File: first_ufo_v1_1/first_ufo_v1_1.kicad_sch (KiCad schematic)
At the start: 66 parts, among them J2 Barrel_Jack_Switch, Q1 2N3904, SW1 SMTS-102, SW2 SMTS-102, SW3 SMTS-102, U1 40106, U3 LM358

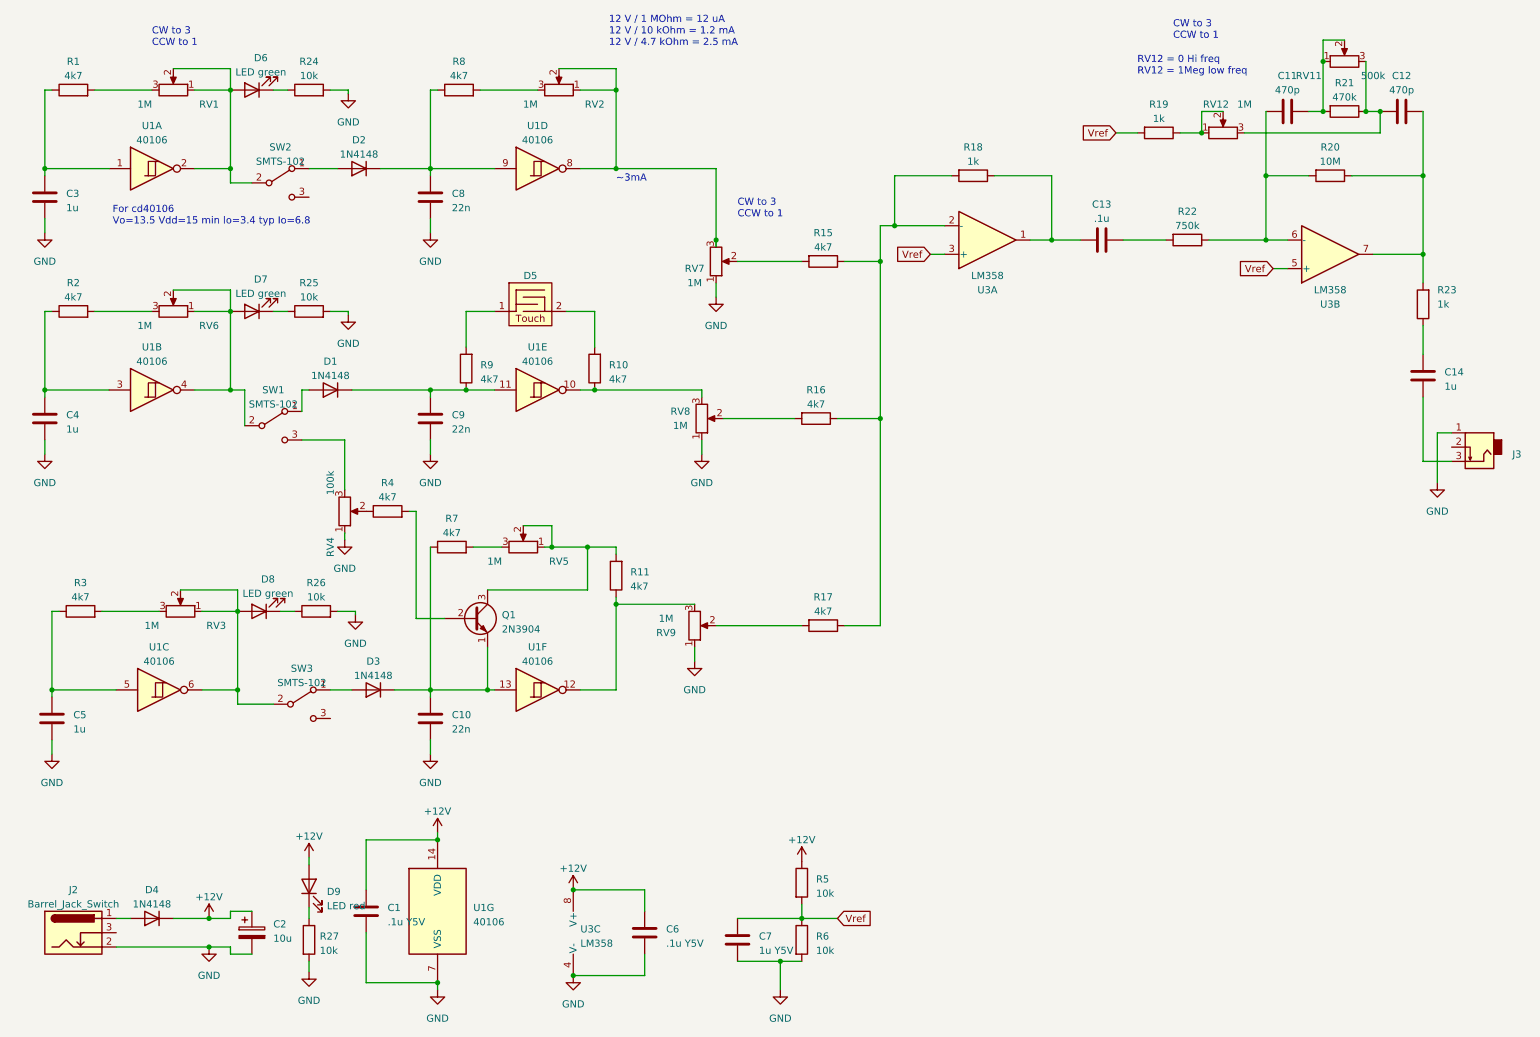
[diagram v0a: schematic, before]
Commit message: edit R15 16 17 to 27k for do not affect on freq in max volume edit RV7 8 9 for better control of volume. coz it use volatge divider now change filter for better control and range fix adder circuit. make on voltage divivder
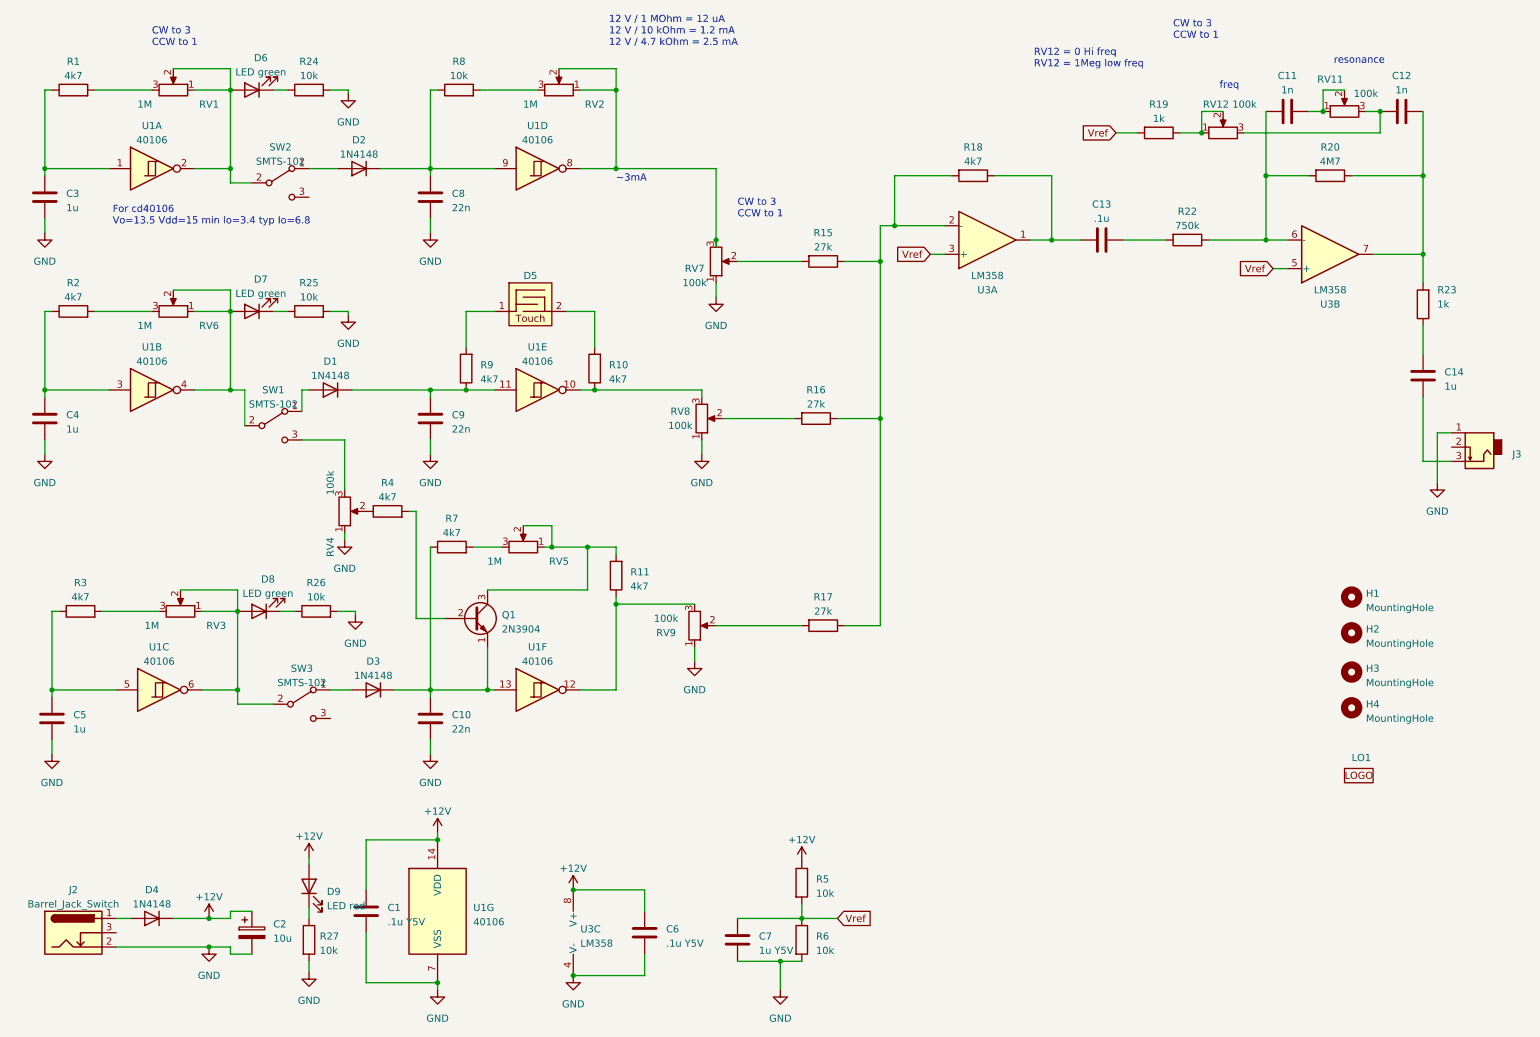
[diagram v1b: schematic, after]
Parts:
- removed R21: 470k, Resistor_THT:R_Axial_DIN0207_L6.3mm_D2.5mm_P10.16mm_Horizontal, symbol Device:R
- added H1, H2, H3, H4: MountingHole, MountingHole:MountingHole_3.2mm_M3, symbol Mechanical:MountingHole
- added LO1: ~, Symbol:Polarity_Center_Positive_6mm_SilkScreen, symbol Graphic:logo_x
- C11, C12: value 470p -> 1n
- R15, R16, R17: value 4k7 -> 27k
- R18: value 1k -> 4k7
- R20: value 10M -> 4M7
- R8: value 4k7 -> 10k
- RV11: value 500k -> 100k
- RV12, RV7, RV8, RV9: value 1M -> 100k
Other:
- note added: "freq"
- note added: "resonance"
- moved on the sheet: RV11

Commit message: no message
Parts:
- added RV10: 1M, Potentiometer_THT:Potentiometer_Bourns_PTV09A-1_Single_Vertical, symbol Device:R_Potentiometer
- LO1: footprint Symbol:Polarity_Center_Positive_6mm_SilkScreen -> Import:Polarity_Center_Positive_3mm_SilkScreen
- R1, R2, R3: value 4k7 -> 27k
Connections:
- net GND: now also RV10.1
- net at R22.2: now also RV10.2; no longer C13.2
- new net: C13.2, RV10.3
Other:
- moved on the sheet: R22
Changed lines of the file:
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@@
     (stroke (width 0) (type default))
   )
-  (wire (pts (xy 213.36 54.61) (xy 220.98 54.61))
-    (stroke (width 0) (type default))
-  )
   (wire (pts (xy 55.88 137.16) (xy 62.23 137.16))
     (stroke (width 0) (type default))
@@
     (stroke (width 0) (type default))
   )
+  (wire (pts (xy 222.25 54.61) (xy 226.06 54.61))
+    (stroke (width 0) (type default))
+  )
   (wire (pts (xy 96.52 81.28) (xy 90.17 81.28))
     (stroke (width 0) (type default))
@@
     (stroke (width 0) (type default))
   )
+  (wire (pts (xy 222.25 60.325) (xy 222.25 54.61))
+    (stroke (width 0) (type default))
+  )
   (wire (pts (xy 22.86 143.51) (xy 22.86 146.05))
     (stroke (width 0) (type default))
@@
     (stroke (width 0) (type default))
   )
+  (wire (pts (xy 216.535 56.515) (xy 216.535 54.61))
+    (stroke (width 0) (type default))
+  )
   (wire (pts (xy 100.33 127) (xy 100.33 134.62))
     (stroke (width 0) (type default))
@@
     (stroke (width 0) (type default))
   )
+  (wire (pts (xy 216.535 54.61) (xy 213.36 54.61))
+    (stroke (width 0) (type default))
+  )
   (wire (pts (xy 119.38 81.28) (xy 138.43 81.28))
     (stroke (width 0) (type default))
@@
     (stroke (width 0) (type default))
   )
+  (wire (pts (xy 216.535 64.135) (xy 216.535 66.675))
+    (stroke (width 0) (type default))
+  )
   (wire (pts (xy 179.07 57.15) (xy 181.61 57.15))
     (stroke (width 0) (type default))
@@
     (stroke (width 0) (type default))
   )
+  (wire (pts (xy 220.345 60.325) (xy 222.25 60.325))
+    (stroke (width 0) (type default))
+  )
   (wire (pts (xy 248.92 27.94) (xy 248.92 31.75))
     (stroke (width 0) (type default))
@@
     (stroke (width 0) (type default))
   )
-  (wire (pts (xy 228.6 54.61) (xy 238.76 54.61))
+  (wire (pts (xy 233.68 54.61) (xy 238.76 54.61))
     (stroke (width 0) (type default))
   )
@@
     )
   )
+  (symbol (lib_id "power:GND") (at 216.535 66.675 0) (unit 1)
+    (in_bom yes) (on_board yes) (dnp no) (fields_autoplaced)
+    (property "Reference" "#PWR025" (at 216.535 73.025 0)
+      (effects (font (size 1.27 1.27)) hide)
+    )
+    (property "Value" "GND" (at 216.535 71.755 0)
+      (effects (font (size 1.27 1.27)))
+    )
+    (property "Footprint" "" (at 216.535 66.675 0)
+      (effects (font (size 1.27 1.27)) hide)
+    )
+    (property "Datasheet" "" (at 216.535 66.675 0)
+      (effects (font (size 1.27 1.27)) hide)
+    )
+    (pin "1")
+    (instances
+      (project "first_ufo_v1_1"
+        (path "/a2b6e046-e043-43da-b3f2-44bda2457408"
+          (reference "#PWR025") (unit 1)
+        )
+      )
+    )
+  )
   (symbol (lib_id "Device:R") (at 93.98 109.22 90) (unit 1)
     (in_bom yes) (on_board yes) (dnp no) (fields_autoplaced)
@@
     )
   )
-  (symbol (lib_id "Device:R") (at 224.79 54.61 270) (unit 1)
+  (symbol (lib_id "Device:R_Potentiometer") (at 216.535 60.325 0) (mirror x) (unit 1)
+    (in_bom yes) (on_board yes) (dnp no)
+    (property "Reference" "RV10" (at 212.725 61.595 0)
+      (effects (font (size 1.27 1.27)))
+    )
+    (property "Value" "1M" (at 212.725 64.135 0)
+      (effects (font (size 1.27 1.27)))
+    )
+    (property "Footprint" "Potentiometer_THT:Potentiometer_Bourns_PTV09A-1_Single_Vertical" (at 216.535 60.325 0)
+      (effects (font (size 1.27 1.27)) hide)
+    )
+    (property "Datasheet" "~" (at 216.535 60.325 0)
+      (effects (font (size 1.27 1.27)) hide)
+    )
+    (pin "1")
+    (pin "2")
+    (pin "3")
+    (instances
+      (project "first_ufo_v1_1"
+        (path "/a2b6e046-e043-43da-b3f2-44bda2457408"
+          (reference "RV10") (unit 1)
+        )
+      )
+    )
+  )
+  (symbol (lib_id "Device:R") (at 229.87 54.61 270) (unit 1)
     (in_bom yes) (on_board yes) (dnp no) (fields_autoplaced)
-    (property "Reference" "R22" (at 224.79 49.53 90)
+    (property "Reference" "R22" (at 229.87 49.53 90)
       (effects (font (size 1.27 1.27)))
     )
-    (property "Value" "750k" (at 224.79 52.07 90)
+    (property "Value" "750k" (at 229.87 52.07 90)
       (effects (font (size 1.27 1.27)))
     )
-    (property "Footprint" "Resistor_THT:R_Axial_DIN0207_L6.3mm_D2.5mm_P10.16mm_Horizontal" (at 224.79 52.832 90)
+    (property "Footprint" "Resistor_THT:R_Axial_DIN0207_L6.3mm_D2.5mm_P10.16mm_Horizontal" (at 229.87 52.832 90)
       (effects (font (size 1.27 1.27)) hide)
     )
-    (property "Datasheet" "~" (at 224.79 54.61 0)
+    (property "Datasheet" "~" (at 229.87 54.61 0)
       (effects (font (size 1.27 1.27)) hide)
     )
@@
       (effects (font (size 1.27 1.27)))
     )
-    (property "Value" "4k7" (at 27.94 118.11 90)
+    (property "Value" "27k" (at 27.94 118.11 90)
       (effects (font (size 1.27 1.27)))
     )
@@
       (effects (font (size 1.27 1.27)))
     )
-    (property "Value" "4k7" (at 26.67 64.77 90)
+    (property "Value" "27k" (at 26.67 64.77 90)
       (effects (font (size 1.27 1.27)))
     )
@@
       (effects (font (size 1.27 1.27)))
     )
-    (property "Footprint" "Symbol:Polarity_Center_Positive_6mm_SilkScreen" (at 255.27 149.86 0)
+    (property "Footprint" "Import:Polarity_Center_Positive_3mm_SilkScreen" (at 255.27 149.86 0)
       (effects (font (size 1.27 1.27)) hide)
     )
@@
       (effects (font (size 1.27 1.27)))
     )
-    (property "Value" "4k7" (at 26.67 25.4 90)
+    (property "Value" "27k" (at 26.67 25.4 90)
       (effects (font (size 1.27 1.27)))
     )
